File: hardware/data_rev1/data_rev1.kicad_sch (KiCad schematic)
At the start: 2 parts, among them J1 BOARD, U1 Pico

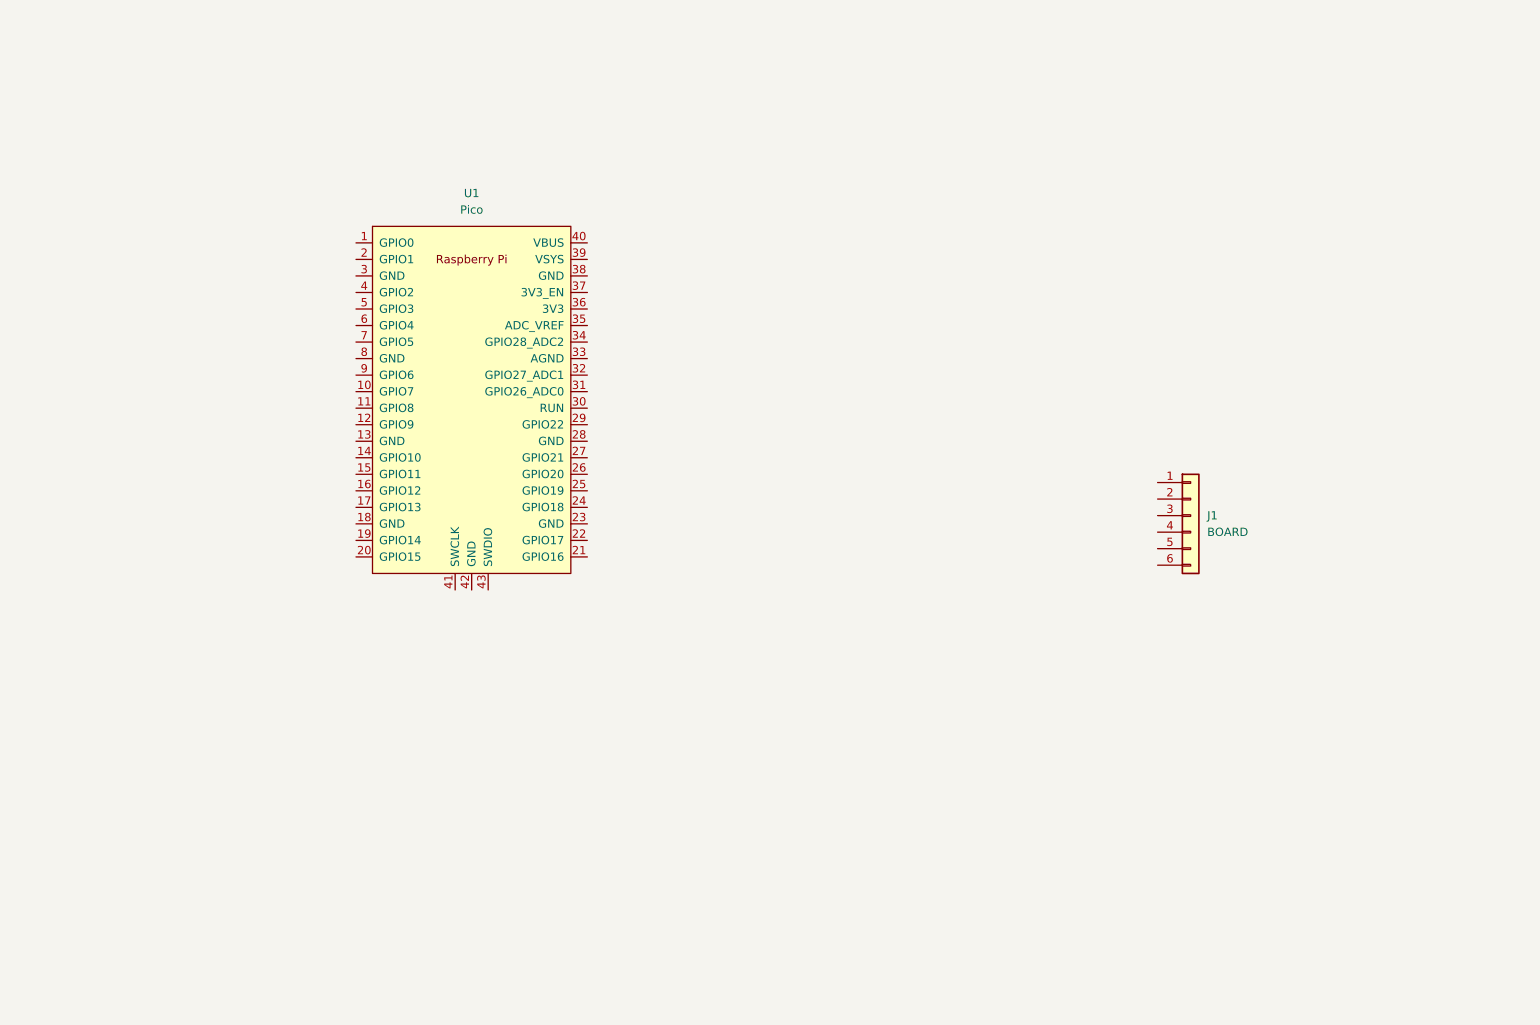
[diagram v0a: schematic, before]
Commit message: Added subsheets for rev 1
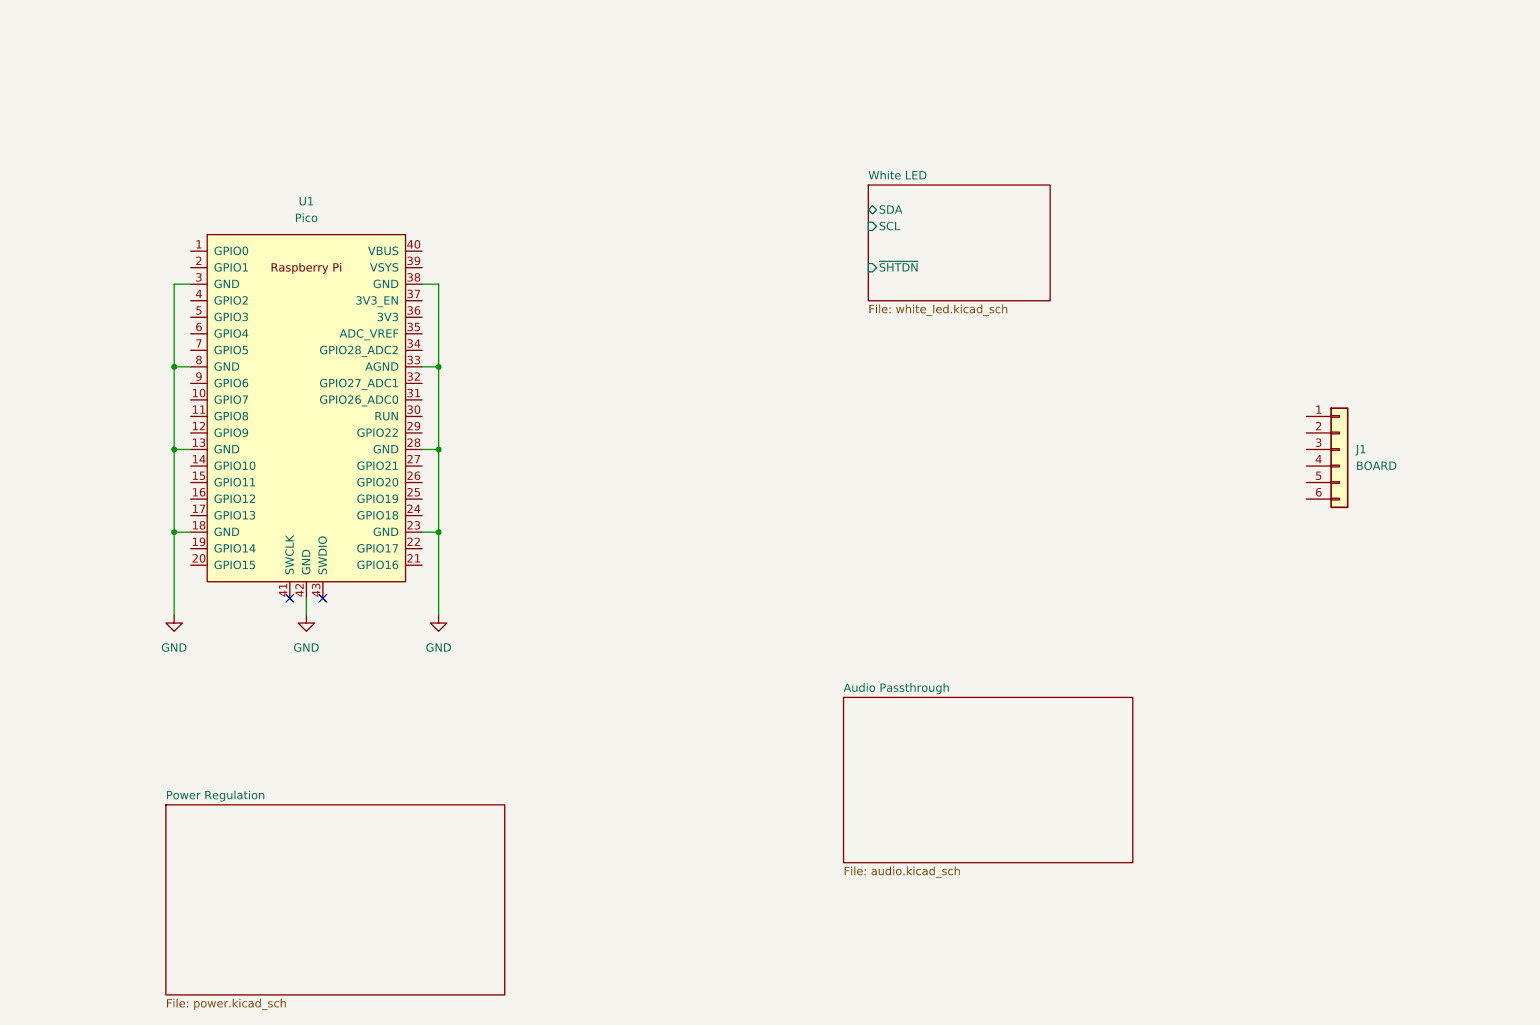
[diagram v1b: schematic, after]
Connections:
- net GND: now reaches U1.13 (GND)
- net GND: now also U1.18 (GND), U1.23 (GND), U1.28 (GND), U1.3 (GND), U1.33 (AGND), U1.38 (GND), U1.42 (GND), U1.8 (GND)
- no-connect marks 0 -> 2
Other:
- added sheet Audio Passthrough (audio.kicad_sch)
- added sheet Power Regulation (power.kicad_sch)
- added sheet White LED (white_led.kicad_sch)
- moved on the sheet: J1, U1
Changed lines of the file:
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@@
     (company "Savo Bajic")
   )
-  (symbol (lib_id "RPi_Pico:Pico") (at 92.71 82.55 0) (unit 1)
-    (in_bom yes) (on_board yes) (dnp no) (fields_autoplaced)
-    (property "Reference" "U1" (at 92.71 50.8 0)
-      (effects (font (size 1.27 1.27)))
-    )
-    (property "Value" "Pico" (at 92.71 53.34 0)
-      (effects (font (size 1.27 1.27)))
-    )
-    (property "Footprint" "RPi_Pico:RPi_Pico_SMD" (at 92.71 82.55 90)
-      (effects (font (size 1.27 1.27)) hide)
-    )
-    (property "Datasheet" "" (at 92.71 82.55 0)
+  (junction (at 87.63 90.17) (diameter 0) (color 0 0 0 0)
+  )
+  (junction (at 46.99 77.47) (diameter 0) (color 0 0 0 0)
+  )
+  (junction (at 46.99 90.17) (diameter 0) (color 0 0 0 0)
+  )
+  (junction (at 87.63 77.47) (diameter 0) (color 0 0 0 0)
+  )
+  (junction (at 46.99 102.87) (diameter 0) (color 0 0 0 0)
+  )
+  (junction (at 87.63 102.87) (diameter 0) (color 0 0 0 0)
+  )
+  (no_connect (at 69.85 113.03))
+  (no_connect (at 64.77 113.03))
+  (wire (pts (xy 87.63 90.17) (xy 87.63 102.87))
+    (stroke (width 0) (type default))
+  )
+  (wire (pts (xy 46.99 102.87) (xy 49.53 102.87))
+    (stroke (width 0) (type default))
+  )
+  (wire (pts (xy 85.09 90.17) (xy 87.63 90.17))
+    (stroke (width 0) (type default))
+  )
+  (wire (pts (xy 46.99 77.47) (xy 49.53 77.47))
+    (stroke (width 0) (type default))
+  )
+  (wire (pts (xy 85.09 77.47) (xy 87.63 77.47))
+    (stroke (width 0) (type default))
+  )
+  (wire (pts (xy 46.99 77.47) (xy 46.99 64.77))
+    (stroke (width 0) (type default))
+  )
+  (wire (pts (xy 67.31 113.03) (xy 67.31 115.57))
+    (stroke (width 0) (type default))
+  )
+  (wire (pts (xy 87.63 64.77) (xy 87.63 77.47))
+    (stroke (width 0) (type default))
+  )
+  (wire (pts (xy 85.09 102.87) (xy 87.63 102.87))
+    (stroke (width 0) (type default))
+  )
+  (wire (pts (xy 46.99 90.17) (xy 49.53 90.17))
+    (stroke (width 0) (type default))
+  )
+  (wire (pts (xy 87.63 77.47) (xy 87.63 90.17))
+    (stroke (width 0) (type default))
+  )
+  (wire (pts (xy 87.63 102.87) (xy 87.63 115.57))
+    (stroke (width 0) (type default))
+  )
+  (wire (pts (xy 46.99 102.87) (xy 46.99 90.17))
+    (stroke (width 0) (type default))
+  )
+  (wire (pts (xy 46.99 90.17) (xy 46.99 77.47))
+    (stroke (width 0) (type default))
+  )
+  (wire (pts (xy 46.99 64.77) (xy 49.53 64.77))
+    (stroke (width 0) (type default))
+  )
+  (wire (pts (xy 46.99 115.57) (xy 46.99 102.87))
+    (stroke (width 0) (type default))
+  )
+  (wire (pts (xy 85.09 64.77) (xy 87.63 64.77))
+    (stroke (width 0) (type default))
+  )
+  (symbol (lib_id "power:GND") (at 67.31 115.57 0) (unit 1)
+    (in_bom yes) (on_board yes) (dnp no) (fields_autoplaced)
+    (property "Reference" "#PWR013" (at 67.31 121.92 0)
+      (effects (font (size 1.27 1.27)) hide)
+    )
+    (property "Value" "GND" (at 67.31 120.65 0)
+      (effects (font (size 1.27 1.27)))
+    )
+    (property "Footprint" "" (at 67.31 115.57 0)
+      (effects (font (size 1.27 1.27)) hide)
+    )
+    (property "Datasheet" "" (at 67.31 115.57 0)
+      (effects (font (size 1.27 1.27)) hide)
+    )
+    (pin "1")
+    (instances
+      (project "data_rev1"
+        (path "/fa6829fa-bbc1-45d3-82a1-c2163374352a"
+          (reference "#PWR013") (unit 1)
+        )
+      )
+    )
+  )
+  (symbol (lib_id "power:GND") (at 46.99 115.57 0) (unit 1)
+    (in_bom yes) (on_board yes) (dnp no) (fields_autoplaced)
+    (property "Reference" "#PWR014" (at 46.99 121.92 0)
+      (effects (font (size 1.27 1.27)) hide)
+    )
+    (property "Value" "GND" (at 46.99 120.65 0)
+      (effects (font (size 1.27 1.27)))
+    )
+    (property "Footprint" "" (at 46.99 115.57 0)
+      (effects (font (size 1.27 1.27)) hide)
+    )
+    (property "Datasheet" "" (at 46.99 115.57 0)
+      (effects (font (size 1.27 1.27)) hide)
+    )
+    (pin "1")
+    (instances
+      (project "data_rev1"
+        (path "/fa6829fa-bbc1-45d3-82a1-c2163374352a"
+          (reference "#PWR014") (unit 1)
+        )
+      )
+    )
+  )
+  (symbol (lib_id "power:GND") (at 87.63 115.57 0) (unit 1)
+    (in_bom yes) (on_board yes) (dnp no) (fields_autoplaced)
+    (property "Reference" "#PWR015" (at 87.63 121.92 0)
+      (effects (font (size 1.27 1.27)) hide)
+    )
+    (property "Value" "GND" (at 87.63 120.65 0)
+      (effects (font (size 1.27 1.27)))
+    )
+    (property "Footprint" "" (at 87.63 115.57 0)
+      (effects (font (size 1.27 1.27)) hide)
+    )
+    (property "Datasheet" "" (at 87.63 115.57 0)
+      (effects (font (size 1.27 1.27)) hide)
+    )
+    (pin "1")
+    (instances
+      (project "data_rev1"
+        (path "/fa6829fa-bbc1-45d3-82a1-c2163374352a"
+          (reference "#PWR015") (unit 1)
+        )
+      )
+    )
+  )
+  (symbol (lib_id "RPi_Pico:Pico") (at 67.31 83.82 0) (unit 1)
+    (in_bom yes) (on_board yes) (dnp no) (fields_autoplaced)
+    (property "Reference" "U1" (at 67.31 52.07 0)
+      (effects (font (size 1.27 1.27)))
+    )
+    (property "Value" "Pico" (at 67.31 54.61 0)
+      (effects (font (size 1.27 1.27)))
+    )
+    (property "Footprint" "RPi_Pico:RPi_Pico_SMD" (at 67.31 83.82 90)
+      (effects (font (size 1.27 1.27)) hide)
+    )
+    (property "Datasheet" "" (at 67.31 83.82 0)
       (effects (font (size 1.27 1.27)) hide)
     )
@@
     )
   )
-  (symbol (lib_id "Connector_Generic:Conn_01x06") (at 203.2 100.33 0) (unit 1)
+  (symbol (lib_id "Connector_Generic:Conn_01x06") (at 226.06 90.17 0) (unit 1)
     (in_bom no) (on_board yes) (dnp no) (fields_autoplaced)
-    (property "Reference" "J1" (at 205.74 100.33 0)
-      (effects (font (size 1.27 1.27)) (justify left))
-    )
-    (property "Value" "BOARD" (at 205.74 102.87 0)
-      (effects (font (size 1.27 1.27)) (justify left))
-    )
-    (property "Footprint" "logo:fill" (at 203.2 100.33 0)
-      (effects (font (size 1.27 1.27)) hide)
-    )
-    (property "Datasheet" "~" (at 203.2 100.33 0)
+    (property "Reference" "J1" (at 228.6 90.17 0)
+      (effects (font (size 1.27 1.27)) (justify left))
+    )
+    (property "Value" "BOARD" (at 228.6 92.71 0)
+      (effects (font (size 1.27 1.27)) (justify left))
+    )
+    (property "Footprint" "logo:fill" (at 226.06 90.17 0)
+      (effects (font (size 1.27 1.27)) hide)
+    )
+    (property "Datasheet" "~" (at 226.06 90.17 0)
       (effects (font (size 1.27 1.27)) hide)
     )
@@
       )
     )
+  )
+  (sheet (at 149.86 128.27) (size 44.45 25.4) (fields_autoplaced)
+    (stroke (width 0.1524) (type solid))
+    (fill (color 0 0 0 0.0000))
+    (property "Sheetname" "Audio Passthrough" (at 149.86 127.5584 0)
+      (effects (font (size 1.27 1.27)) (justify left bottom))
+    )
+    (property "Sheetfile" "audio.kicad_sch" (at 149.86 154.2546 0)
+      (effects (font (size 1.27 1.27)) (justify left top))
+    )
+    (instances
+      (project "data_rev1"
+        (path "/fa6829fa-bbc1-45d3-82a1-c2163374352a" (page "3"))
+      )
+    )
+  )
+  (sheet (at 153.67 49.53) (size 27.94 17.78) (fields_autoplaced)
+    (stroke (width 0.1524) (type solid))
+    (fill (color 0 0 0 0.0000))
+    (property "Sheetname" "White LED" (at 153.67 48.8184 0)
+      (effects (font (size 1.27 1.27)) (justify left bottom))
+    )
+    (property "Sheetfile" "white_led.kicad_sch" (at 153.67 67.8946 0)
+      (effects (font (size 1.27 1.27)) (justify left top))
+    )
+    (pin "SDA" bidirectional (at 153.67 53.34 180)
+      (effects (font (size 1.27 1.27)) (justify left))
+    )
+    (pin "SCL" input (at 153.67 55.88 180)
+      (effects (font (size 1.27 1.27)) (justify left))
+    )
+    (pin "~{SHTDN}" input (at 153.67 62.23 180)
+      (effects (font (size 1.27 1.27)) (justify left))
+    )
+    (instances
+      (project "data_rev1"
+        (path "/fa6829fa-bbc1-45d3-82a1-c2163374352a" (page "2"))
+      )
+    )
+  )
+  (sheet (at 45.72 144.78) (size 52.07 29.21) (fields_autoplaced)
+    (stroke (width 0.1524) (type solid))
+    (fill (color 0 0 0 0.0000))
+    (property "Sheetname" "Power Regulation" (at 45.72 144.0684 0)
+      (effects (font (size 1.27 1.27)) (justify left bottom))
+    )
+    (property "Sheetfile" "power.kicad_sch" (at 45.72 174.5746 0)
+      (effects (font (size 1.27 1.27)) (justify left top))
+    )
+    (instances
+      (project "data_rev1"
+        (path "/fa6829fa-bbc1-45d3-82a1-c2163374352a" (page "4"))
+      )
+    )

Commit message: Initial layout and circuit
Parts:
- added C1: 0u1, Capacitor_SMD:C_0603_1608Metric, symbol Device:C
- added C2, C3: 10u, Resistor_SMD:R_0805_2012Metric, symbol Device:C
- added C4: 1u, Capacitor_SMD:C_0603_1608Metric, symbol Device:C
- added D1, D2, D3: STAT, LED_SMD:LED_0805_2012Metric, symbol Device:LED
- added J1, J2: AudioJack3, Connector_Audio:Jack_3.5mm_CUI_SJ-3523-SMT_Horizontal, symbol Connector_Audio:AudioJack3
- added R1, R2, R3, R4: 51k, Resistor_SMD:R_0603_1608Metric, symbol Device:R
- added R5, R6: 5k1, Resistor_SMD:R_0603_1608Metric, symbol Device:R
- added R7, R8, R9: 130, Resistor_SMD:R_0603_1608Metric, symbol Device:R
- added SW1, SW2, SW3: PTS636, Button_Switch_SMD:SW_SPST_CK_RS282G05A3, symbol Switch:SW_Push
- added U1: CAP1206-x-AIA, Package_DFN_QFN:DFN-10-1EP_3x3mm_P0.5mm_EP1.55x2.48mm, symbol Sensor_Touch:CAP1206-x-AIA
- renumbered J1 to J3, U1 to U2
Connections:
- net GND: now also C1.2, C4.1, J1.S, J2.S, R2.2, R4.2, R7.2, R8.2, R9.2, SW1.2, SW2.2, SW3.2, U1.11 (GND), U1.2 (ALERT#)
- net SDA: now reaches U2.1 (GPIO0)
- net SDA: now also R5.2, U1.3 (SMDATA)
- net SCL: now reaches U2.2 (GPIO1)
- net SCL: now also R6.2, U1.4 (SMCLK)
- net ~{SHTDN}_{1}: now reaches U2.20 (GPIO15)
- net ~{SHTDN}_{2}: now reaches U2.21 (GPIO16)
- net LED_{1}: now reaches U2.22 (GPIO17)
- net LED_{1}: now also D1.2 (A)
- net LED_{2}: now reaches U2.24 (GPIO18)
- net LED_{2}: now also D2.2 (A)
- net LED_{3}: now reaches U2.25 (GPIO19)
- net LED_{3}: now also D3.2 (A)
- net BUT_{1}: now reaches U2.26 (GPIO20)
- net BUT_{1}: now also SW1.1
- net BUT_{2}: now reaches U2.27 (GPIO21)
- net BUT_{2}: now also SW2.1
- net RUN: now reaches U2.30 (RUN)
- net RUN: now also SW3.1
- net RIGHT: now reaches U2.31 (GPIO26_ADC0)
- net RIGHT: now also C3.1, R3.2, R4.1
- net LEFT: now reaches U2.32 (GPIO27_ADC1)
- net LEFT: now also C2.1, R1.2, R2.1
- net +3V3: now reaches U2.36 (3V3)
- net +3V3: now also C1.1, C4.2, R1.1, R3.1, R5.1, R6.1, U1.5 (VDD)
- net PAD_{0}: now reaches J3.1 (Pin_1)
- net PAD_{0}: now also U1.9 (CS3)
- net PAD_{1}: now reaches J3.2 (Pin_2)
- net PAD_{1}: now also U1.10 (CS2)
- net PAD_{2}: now reaches J3.3 (Pin_3)
- net PAD_{2}: now also U1.1 (CS1)
- net PAD_{3}: now reaches J3.4 (Pin_4)
- net PAD_{3}: now also U1.8 (CS4)
- net PAD_{DA}: now reaches J3.5 (Pin_5)
- net PAD_{DA}: now also U1.7 (CS5)
- net PAD_{TA}: now reaches J3.6 (Pin_6)
- net PAD_{TA}: now also U1.6 (CS6)
- new net: D3.1 (K), R9.1
- new net: D2.1 (K), R8.1
- new net: D1.1 (K), R7.1
- new net LEFT_{RAW}: C2.2, J1.T, J2.T
- new net RIGHT_{RAW}: C3.2, J1.R, J2.R
- no-connect marks 2 -> 21
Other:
- removed sheet Audio Passthrough
- removed sheet Power Regulation
- sheet White LED ports: added ~{SHTDN}_{1}, ~{SHTDN}_{2}; removed ~{SHTDN}
- note added: "A couple status LEDs and buttons are always nice to have"
- note added: "Audio interface"
- note added: "Capacitive sensing for the front face"
- note added: "Two jacks to act as a passthrough that gets tapped"
- moved on the sheet: J3, U2
